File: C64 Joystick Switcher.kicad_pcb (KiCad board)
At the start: 2 copper layers, 49.3 x 81.5 mm, 31 parts, among them J1 Port 1, J2 Port 2, J3 Mega Drive, J4 B2_SEL, J5 B1_SEL, Q1 BC547, SW1 P1_SEL, SW2 P2_SEL, U1 74HCT4053, U2 74HCT4053, U3 NE555, U4 NE555

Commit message: Gerber export
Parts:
- J3: value Mega Drive -> Joystick
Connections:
- J3 pad 5: VCC -> (no net)
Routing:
- net VCC: track 283.9 -> 275.8 mm
- net /GP_BTN_2: track 15.2 -> 17.0 mm
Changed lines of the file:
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@@
 (kicad_pcb (version 4) (host pcbnew 4.0.7)
   (general
-    (links 98)
+    (links 97)
     (no_connects 0)
     (area 97.968999 35.484999 147.395001 117.137001)
     (thickness 1.6)
     (drawings 89)
-    (tracks 683)
+    (tracks 681)
     (zones 0)
     (modules 31)
@@
       (effects (font (size 1 1) (thickness 0.15)))
     )
-    (fp_text value "Mega Drive" (at 5.54 18.44) (layer F.Fab)
+    (fp_text value Joystick (at 5.54 18.44) (layer F.Fab)
       (effects (font (size 1 1) (thickness 0.15)))
     )
@@
     (pad 4 thru_hole circle (at 8.31 0) (size 1.6 1.6) (drill 1) (layers *.Cu *.Mask)
       (net 8 RIGHT))
-    (pad 5 thru_hole circle (at 11.08 0) (size 1.6 1.6) (drill 1) (layers *.Cu *.Mask)
-      (net 4 VCC))
+    (pad 5 thru_hole circle (at 11.08 0) (size 1.6 1.6) (drill 1) (layers *.Cu *.Mask))
     (pad 6 thru_hole circle (at 1.385 2.84) (size 1.6 1.6) (drill 1) (layers *.Cu *.Mask)
       (net 29 /GP_BTN_1))
@@
   (segment (start 146.685 36.83) (end 146.05 36.195) (width 0.25) (layer F.Cu) (net 4))
   (segment (start 127 36.195) (end 140.335 36.195) (width 0.25) (layer F.Cu) (net 4))
-  (segment (start 121.316 106.14) (end 121.19 106.14) (width 0.25) (layer F.Cu) (net 4))
-  (segment (start 121.19 106.14) (end 120.015 107.315) (width 0.25) (layer F.Cu) (net 4))
-  (segment (start 120.015 107.315) (end 116.056 107.315) (width 0.25) (layer F.Cu) (net 4))
-  (segment (start 116.056 107.315) (end 114.391 108.98) (width 0.25) (layer F.Cu) (net 4))
   (segment (start 100.965 83.185) (end 100.965 104.14) (width 0.25) (layer F.Cu) (net 4))
   (segment (start 114.391 110.399) (end 114.391 108.98) (width 0.25) (layer F.Cu) (net 4))
@@
   (segment (start 114.3 95.25) (end 114.3 97.79) (width 0.25) (layer B.Cu) (net 29))
   (segment (start 114.3 97.79) (end 114.3 100.33) (width 0.25) (layer B.Cu) (net 29))
-  (segment (start 122.555 100.33) (end 122.555 106.68) (width 0.25) (layer B.Cu) (net 30))
-  (segment (start 121.285 107.315) (end 119.931 108.669) (width 0.25) (layer B.Cu) (net 30))
-  (segment (start 121.92 107.315) (end 121.285 107.315) (width 0.25) (layer B.Cu) (net 30))
-  (segment (start 122.555 106.68) (end 121.92 107.315) (width 0.25) (layer B.Cu) (net 30))
+  (segment (start 123.19 104.775) (end 123.19 100.965) (width 0.25) (layer B.Cu) (net 30))
+  (segment (start 123.19 100.965) (end 122.555 100.33) (width 0.25) (layer B.Cu) (net 30))
+  (segment (start 123.19 107.95) (end 122.555 108.585) (width 0.25) (layer B.Cu) (net 30))
+  (segment (start 123.19 104.775) (end 123.19 107.95) (width 0.25) (layer B.Cu) (net 30))
+  (segment (start 119.931 108.98) (end 122.16 108.98) (width 0.25) (layer B.Cu) (net 30))
+  (segment (start 122.16 108.98) (end 122.555 108.585) (width 0.25) (layer B.Cu) (net 30))
   (segment (start 119.931 108.669) (end 119.931 108.98) (width 0.25) (layer B.Cu) (net 30))
   (segment (start 122.555 100.33) (end 122.555 97.79) (width 0.25) (layer B.Cu) (net 30))

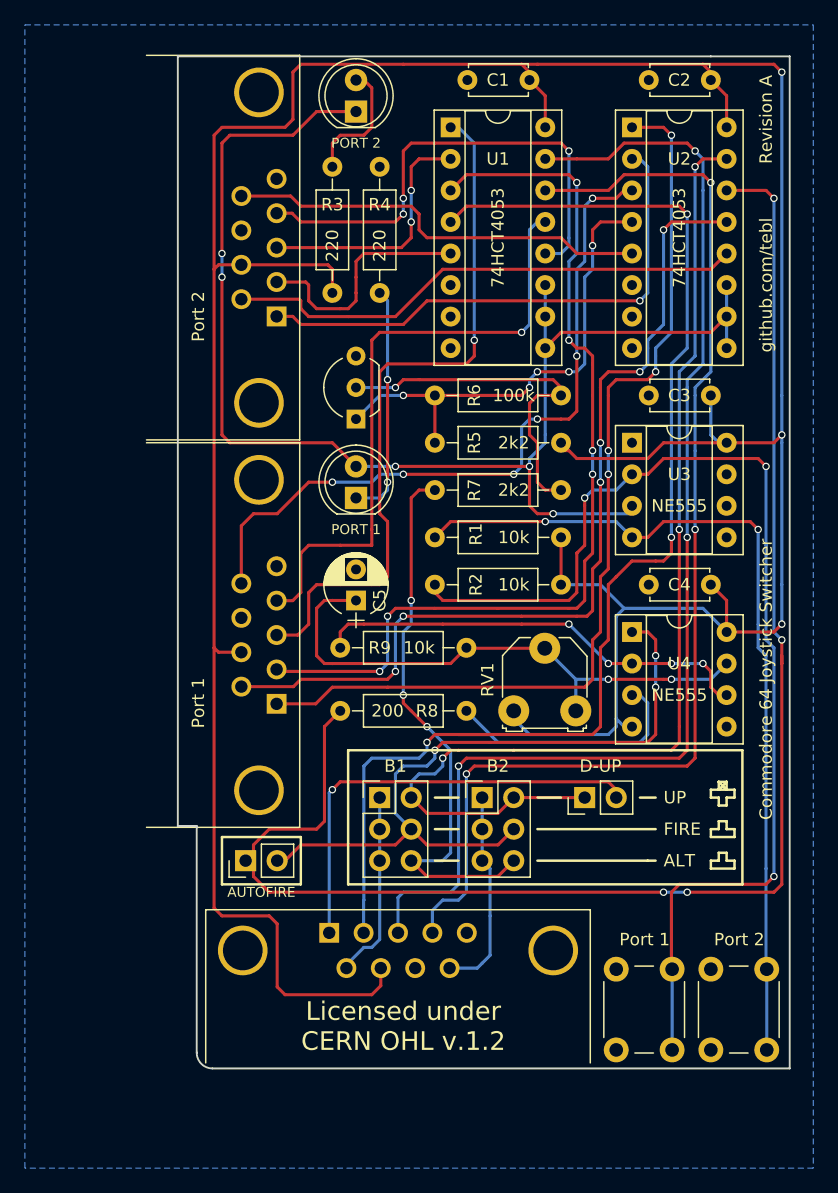
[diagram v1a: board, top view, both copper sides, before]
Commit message: Replace auto-fire circuit
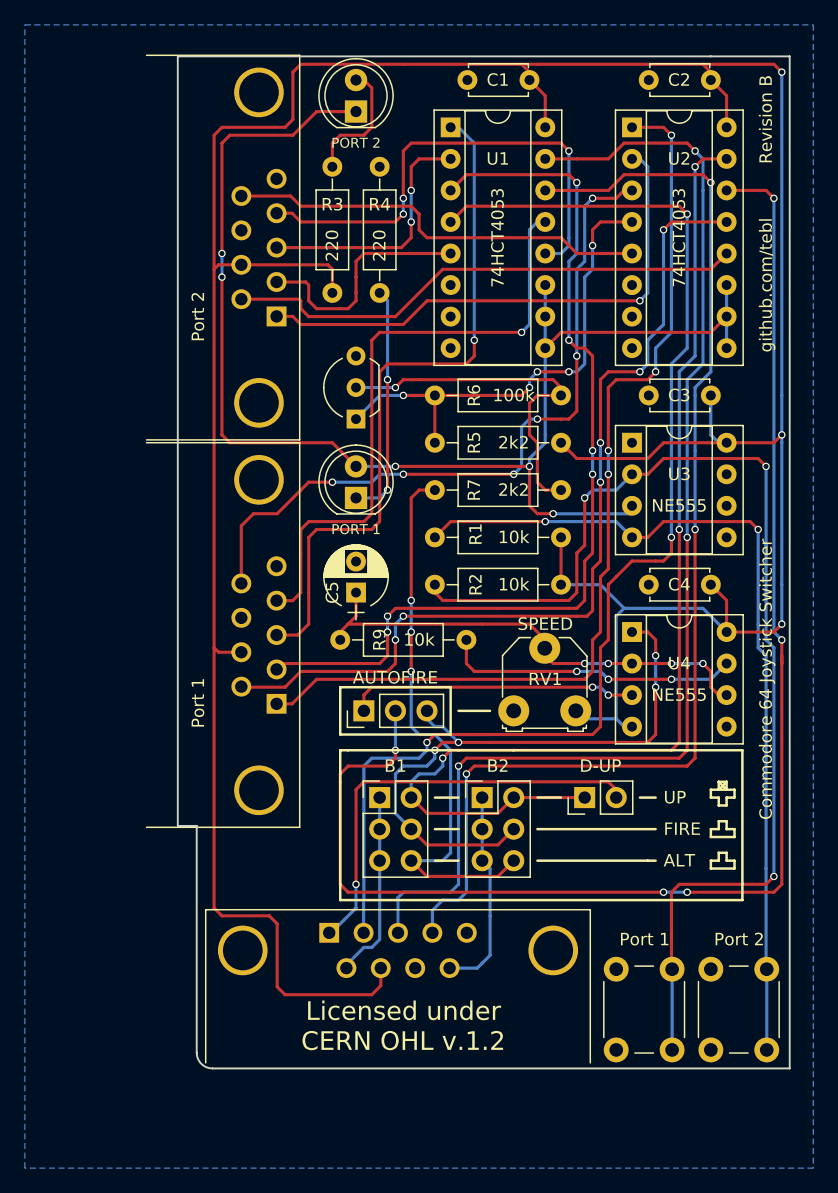
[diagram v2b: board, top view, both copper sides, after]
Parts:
- removed JP3: AUTOFIRE_EN, Pin_Headers:Pin_Header_Straight_1x02_Pitch2.54mm
- removed R8: 200, Resistors_THT:R_Axial_DIN0207_L6.3mm_D2.5mm_P10.16mm_Horizontal
- added JP2: AUTOFIRE, Pin_Headers:Pin_Header_Straight_1x03_Pitch2.54mm, F.Cu at (113.0, 88.3)
- RV1: value 2k -> 10k
- moved C5 0.64 mm to (112.4, 78.7)
- moved R9 0.64 mm to (111.1, 82.5)
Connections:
- R9 pad 1: Net-(R9-Pad1) -> Net-(C5-Pad1)
- R9 pad 2: Net-(C5-Pad1) -> Net-(R9-Pad2)
- RV1 pad 1: VCC -> (no net)
- RV1 pad 3: Net-(C5-Pad1) -> VCC
- U2 pad 14: AUTOFIRE -> Net-(JP2-Pad2)
- U4 pad 2: Net-(R9-Pad1) -> Net-(C5-Pad1)
- U4 pad 3: Net-(R8-Pad1) -> AUTOFIRE
- U4 pad 6: Net-(R9-Pad1) -> Net-(C5-Pad1)
- U4 pad 7: Net-(C5-Pad1) -> Net-(R9-Pad2)
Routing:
- net Net-(JP2-Pad2): track 0.00 -> 114.0 mm, vias 0 -> 5
- net AUTOFIRE: track 122.0 -> 23.4 mm, vias 4 -> 2
- net Net-(R9-Pad1): track 35.8 -> 0.00 mm, vias 4 -> 0
- net Net-(R9-Pad2): track 0.00 -> 23.9 mm, vias 0 -> 3
- net Net-(R8-Pad1): track 20.0 -> 0.00 mm
- net FIRE: track 57.9 -> 50.7 mm, vias 3 -> 4
- net VCC: track 275.8 -> 269.0 mm
- net Net-(C5-Pad1): track 45.2 -> 38.7 mm, vias 2 -> 4
- net /GP_UP: track 35.7 -> 34.6 mm
- net Net-(J1-Pad3): track 56.9 -> 56.0 mm
- net Net-(J1-Pad2): track 75.8 -> 75.3 mm
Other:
- board text added: "ENABLE"
- board text added: "Revision B"
- board text added: "SPEED"
- board text removed: "AUTOFIRE"
- board text removed: "Revision A"

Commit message: Auto-fire should now work
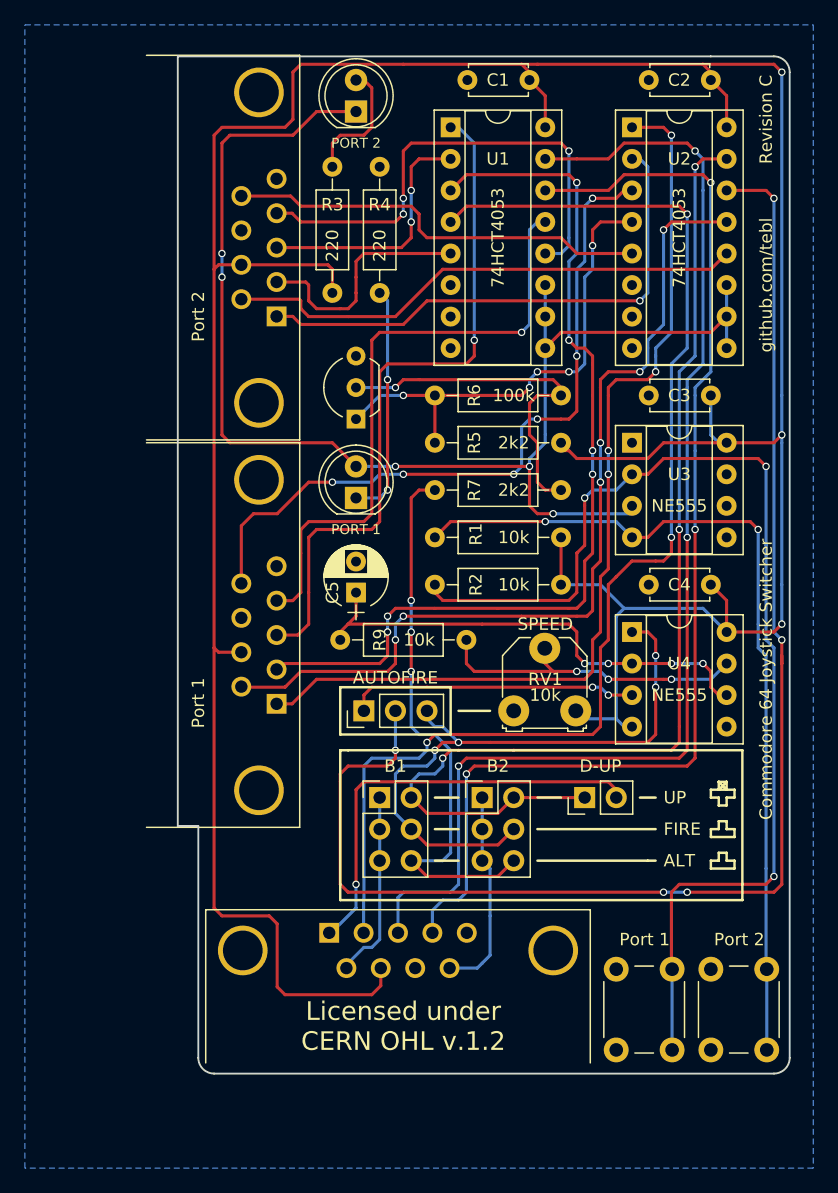
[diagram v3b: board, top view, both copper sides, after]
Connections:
- RV1 pad 2: Net-(C5-Pad1) -> Net-(R9-Pad2)
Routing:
- net Net-(R9-Pad2): track 23.9 -> 26.1 mm
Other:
- board size 49.3 x 81.5 mm -> 49.3 x 81.9 mm
- board text added: "10k"
- board text added: "Revision C"
- board text removed: "Revision B"
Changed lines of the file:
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@@
     (links 95)
     (no_connects 0)
-    (area 97.968999 35.484999 147.395001 117.137001)
+    (area 85.725 33.02 149.225001 125.655)
     (thickness 1.6)
-    (drawings 102)
-    (tracks 691)
+    (drawings 105)
+    (tracks 693)
     (zones 0)
     (modules 30)
@@
     (fp_arc (start 2.5 -2.5) (end 1.1 -1.61) (angle 90) (layer F.Fab) (width 0.1))
     (pad 2 thru_hole circle (at 2.5 -5.04) (size 2.5 2.5) (drill 1.2) (layers *.Cu *.Mask)
-      (net 32 "Net-(C5-Pad1)"))
+      (net 34 "Net-(R9-Pad2)"))
     (pad 3 thru_hole circle (at 5 0) (size 2.5 2.5) (drill 1.2) (layers *.Cu *.Mask)
       (net 4 VCC))
@@
     )
   )
+  (gr_text 10k (at 127.635 86.995) (layer F.SilkS)
+    (effects (font (size 1 1) (thickness 0.15)))
+  )
+  (gr_line (start 99.695 116.205) (end 99.695 97.536) (angle 90) (layer Edge.Cuts) (width 0.15))
+  (gr_arc (start 100.965 116.205) (end 100.965 117.475) (angle 90) (layer Edge.Cuts) (width 0.15))
+  (gr_arc (start 146.05 116.205) (end 147.32 116.205) (angle 90) (layer Edge.Cuts) (width 0.15))
+  (gr_arc (start 146.05 36.83) (end 146.05 35.56) (angle 90) (layer Edge.Cuts) (width 0.15))
   (gr_line (start 120.65 88.265) (end 123.19 88.265) (angle 90) (layer F.SilkS) (width 0.2))
   (gr_text SPEED (at 127.635 81.28) (layer F.SilkS)
@@
     (effects (font (size 1 1) (thickness 0.15)))
   )
-  (gr_text "Revision B" (at 145.415 40.64 90) (layer F.SilkS)
+  (gr_text "Revision C" (at 145.415 40.64 90) (layer F.SilkS)
     (effects (font (size 1 1) (thickness 0.15)))
   )
@@
     (effects (font (size 1 1) (thickness 0.15)))
   )
-  (gr_line (start 147.32 117.062) (end 147.32 35.56) (angle 90) (layer Edge.Cuts) (width 0.15))
-  (gr_line (start 147.32 35.56) (end 140.97 35.56) (angle 90) (layer Edge.Cuts) (width 0.15))
+  (gr_line (start 147.32 116.205) (end 147.32 36.84) (angle 90) (layer Edge.Cuts) (width 0.15))
+  (gr_line (start 146.05 35.56) (end 140.97 35.56) (angle 90) (layer Edge.Cuts) (width 0.15))
   (gr_text D-UP (at 132.08 92.71) (layer F.SilkS)
     (effects (font (size 1 1) (thickness 0.15)))
@@
     (effects (font (size 1.5 1.5) (thickness 0.15)) (justify mirror))
   )
-  (gr_line (start 99.568 97.536) (end 99.568 115.792) (angle 90) (layer Edge.Cuts) (width 0.15))
-  (gr_line (start 100.838 117.062) (end 147.32 117.062) (angle 90) (layer Edge.Cuts) (width 0.15))
-  (gr_arc (start 100.838 115.792) (end 100.838 117.062) (angle 90) (layer Edge.Cuts) (width 0.15))
+  (gr_line (start 100.965 117.475) (end 146.05 117.475) (angle 90) (layer Edge.Cuts) (width 0.15))
   (gr_line (start 140.97 35.56) (end 98.044 35.56) (angle 90) (layer Edge.Cuts) (width 0.15))
   (gr_text "Port 1" (at 135.636 106.68) (layer F.SilkS)
@@
   )
   (gr_line (start 98.044 97.536) (end 98.044 35.56) (angle 90) (layer Edge.Cuts) (width 0.15))
-  (gr_line (start 99.568 97.536) (end 98.044 97.536) (angle 90) (layer Edge.Cuts) (width 0.15))
+  (gr_line (start 99.695 97.536) (end 98.044 97.536) (angle 90) (layer Edge.Cuts) (width 0.15))
   (segment (start 127.635 59.055) (end 127.635 66.04) (width 0.25) (layer B.Cu) (net 1))
   (segment (start 126.365 67.945) (end 126.365 68.58) (width 0.25) (layer B.Cu) (net 1))
@@
   (segment (start 113.03 86.995) (end 113.03 88.265) (width 0.25) (layer F.Cu) (net 31))
   (segment (start 113.665 86.36) (end 113.03 86.995) (width 0.25) (layer F.Cu) (net 31))
-  (segment (start 127.595 83.225) (end 127.595 82.51) (width 0.25) (layer F.Cu) (net 32))
-  (segment (start 127.595 82.51) (end 126.365 81.28) (width 0.25) (layer F.Cu) (net 32))
+  (segment (start 130.81 84.455) (end 130.175 83.82) (width 0.25) (layer F.Cu) (net 32))
+  (via (at 130.81 84.455) (size 0.6) (drill 0.4) (layers F.Cu B.Cu) (net 32))
+  (segment (start 132.715 84.455) (end 130.81 84.455) (width 0.25) (layer B.Cu) (net 32))
+  (via (at 132.715 84.455) (size 0.6) (drill 0.4) (layers F.Cu B.Cu) (net 32))
+  (segment (start 134.62 84.455) (end 132.715 84.455) (width 0.25) (layer F.Cu) (net 32))
+  (segment (start 126.365 81.28) (end 122.555 81.28) (width 0.25) (layer F.Cu) (net 32))
+  (segment (start 113.03 81.28) (end 111.76 81.28) (width 0.25) (layer F.Cu) (net 32))
+  (segment (start 119.38 81.28) (end 122.555 81.28) (width 0.25) (layer F.Cu) (net 32))
   (segment (start 113.03 81.28) (end 119.38 81.28) (width 0.25) (layer F.Cu) (net 32))
-  (segment (start 119.38 81.28) (end 122.555 81.28) (width 0.25) (layer F.Cu) (net 32))
-  (segment (start 113.03 81.28) (end 111.76 81.28) (width 0.25) (layer F.Cu) (net 32))
-  (segment (start 126.365 81.28) (end 122.555 81.28) (width 0.25) (layer F.Cu) (net 32))
-  (segment (start 132.715 84.455) (end 130.81 84.455) (width 0.25) (layer B.Cu) (net 32))
-  (segment (start 128.27 84.455) (end 127.595 83.78) (width 0.25) (layer F.Cu) (net 32))
-  (segment (start 130.81 84.455) (end 128.27 84.455) (width 0.25) (layer F.Cu) (net 32))
-  (via (at 130.81 84.455) (size 0.6) (drill 0.4) (layers F.Cu B.Cu) (net 32))
-  (segment (start 127.595 83.78) (end 127.595 83.225) (width 0.25) (layer F.Cu) (net 32))
+  (segment (start 129.54 81.28) (end 126.365 81.28) (width 0.25) (layer F.Cu) (net 32))
+  (segment (start 130.175 81.915) (end 129.54 81.28) (width 0.25) (layer F.Cu) (net 32))
+  (segment (start 130.175 83.82) (end 130.175 81.915) (width 0.25) (layer F.Cu) (net 32))
   (segment (start 111.125 82.55) (end 111.125 81.915) (width 0.25) (layer F.Cu) (net 32))
   (segment (start 112.395 78.74) (end 112.395 79.375) (width 0.25) (layer F.Cu) (net 32))
@@
   (segment (start 112.395 80.645) (end 111.76 81.28) (width 0.25) (layer F.Cu) (net 32))
   (segment (start 111.76 81.28) (end 111.125 81.915) (width 0.25) (layer F.Cu) (net 32))
-  (segment (start 132.715 84.455) (end 134.62 84.455) (width 0.25) (layer F.Cu) (net 32))
-  (via (at 132.715 84.455) (size 0.6) (drill 0.4) (layers F.Cu B.Cu) (net 32))
   (segment (start 134.62 84.455) (end 137.795 84.455) (width 0.25) (layer F.Cu) (net 32))
   (segment (start 140.97 86.36) (end 141.605 86.995) (width 0.25) (layer F.Cu) (net 32))
@@
   (segment (start 146.685 102.235) (end 146.685 84.455) (width 0.25) (layer F.Cu) (net 33))
   (segment (start 146.685 84.455) (end 146.685 83.82) (width 0.25) (layer F.Cu) (net 33))
+  (segment (start 127.595 83.225) (end 127.595 84.415) (width 0.25) (layer F.Cu) (net 34))
+  (segment (start 127.595 84.415) (end 128.27 85.09) (width 0.25) (layer F.Cu) (net 34))
   (segment (start 121.285 82.55) (end 121.285 84.455) (width 0.25) (layer F.Cu) (net 34))
   (segment (start 140.97 85.725) (end 142.24 84.455) (width 0.25) (layer B.Cu) (net 34))
@@
   (segment (start 132.715 85.725) (end 137.16 85.725) (width 0.25) (layer F.Cu) (net 34))
   (segment (start 132.08 85.09) (end 130.81 85.09) (width 0.25) (layer B.Cu) (net 34))
-  (segment (start 130.175 85.09) (end 121.92 85.09) (width 0.25) (layer F.Cu) (net 34))
+  (segment (start 130.175 85.09) (end 128.27 85.09) (width 0.25) (layer F.Cu) (net 34))
+  (segment (start 128.27 85.09) (end 121.92 85.09) (width 0.25) (layer F.Cu) (net 34))
   (segment (start 121.92 85.09) (end 121.285 84.455) (width 0.25) (layer F.Cu) (net 34))
   (segment (start 132.715 85.725) (end 132.08 85.09) (width 0.25) (layer B.Cu) (net 34))

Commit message: Simplified routing and reduced number of vias by more than 55%
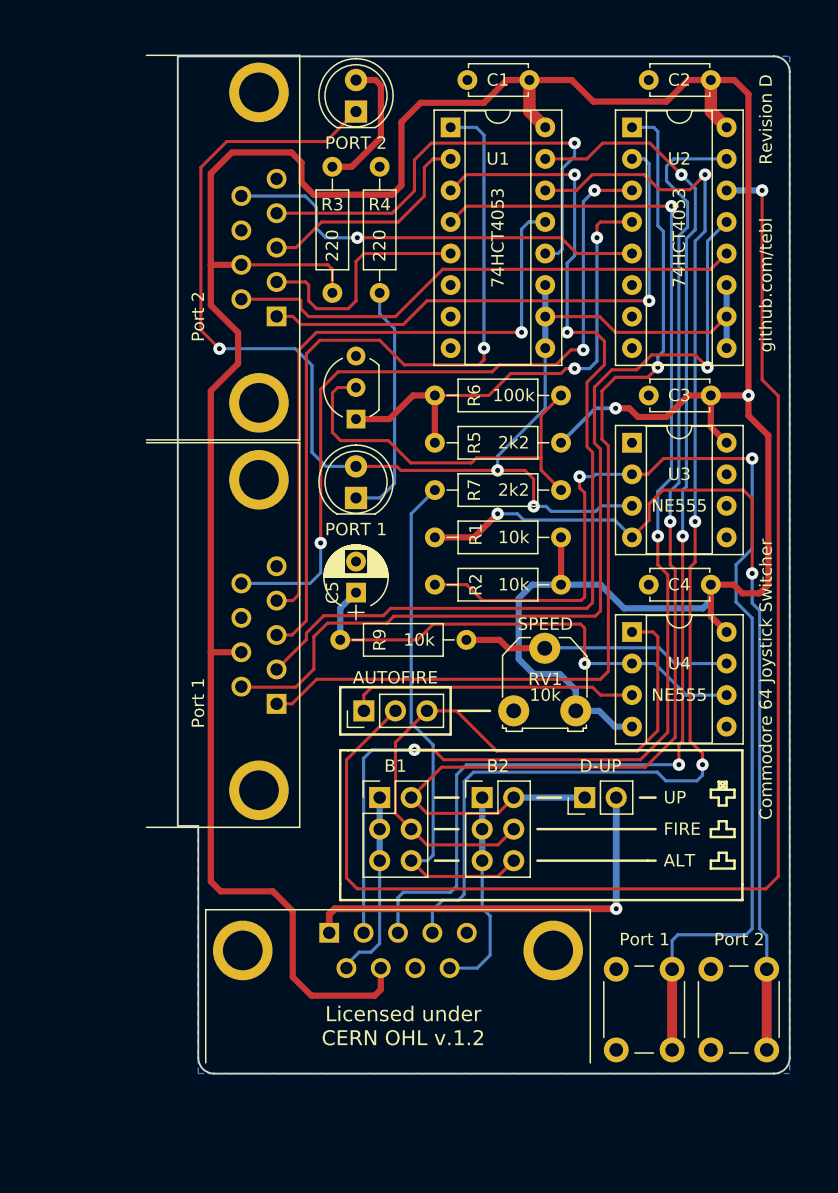
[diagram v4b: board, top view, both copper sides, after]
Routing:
- net Net-(J1-Pad3): track 56.0 -> 61.2 mm
- net Net-(JP2-Pad2): track 114.0 -> 109.3 mm, vias 5 -> 1
- net Net-(R1-Pad1): track 70.1 -> 74.6 mm
- net Net-(R9-Pad2): track 26.1 -> 21.8 mm, vias 3 -> 0
- net Net-(J4-Pad6): track 46.8 -> 42.8 mm, vias 3 -> 0
- net RIGHT: track 95.2 -> 98.2 mm
- net Net-(Q1-Pad2): track 29.3 -> 32.2 mm, vias 1 -> 0
- net PORT: track 108.7 -> 111.0 mm, vias 5 -> 3
- net LEFT: track 98.8 -> 96.5 mm
- net Net-(J2-Pad3): track 20.3 -> 18.3 mm, vias 2 -> 0
- net Net-(J1-Pad9): track 58.4 -> 60.2 mm, vias 6 -> 3
- net Net-(C5-Pad1): track 39.0 -> 40.6 mm, vias 4 -> 1
- net Net-(J1-Pad6): track 72.5 -> 74.1 mm, vias 6 -> 1
- net UP: track 89.3 -> 90.8 mm, vias 3 -> 1
- net Net-(J1-Pad2): track 75.3 -> 76.6 mm, vias 6 -> 2
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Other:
- outline, holes or cut-outs redrawn
- net class Default: clearance 0.2 -> 0.25; via_dia 0.6 -> 0.8
- rule pad_to_mask_clearance: 0.2 -> 0
- rule trace_clearance: 0.2 -> 0.25
- rule trace_min: 0.2 -> 0.25
- rule via_min_size: 0.4 -> 0.8
- board text added: "Revision D"
- board text removed: "Revision C"

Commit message: Small layout improvements
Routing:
- net UP: track 90.8 -> 77.9 mm
- net LEFT: track 96.5 -> 94.2 mm
- net DOWN: track 101.5 -> 100.4 mm
- net Net-(J4-Pad6): track 42.8 -> 42.0 mm
- net RIGHT: track 98.2 -> 97.4 mm
